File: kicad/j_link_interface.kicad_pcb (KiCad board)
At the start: 4 copper layers, 22.5 x 26.2 mm, 9 parts, among them J1 Conn_01x05_Pin, J2 SSW-110-02-G-D-RA-N, J3 FTSH-107-01-X-DV-K

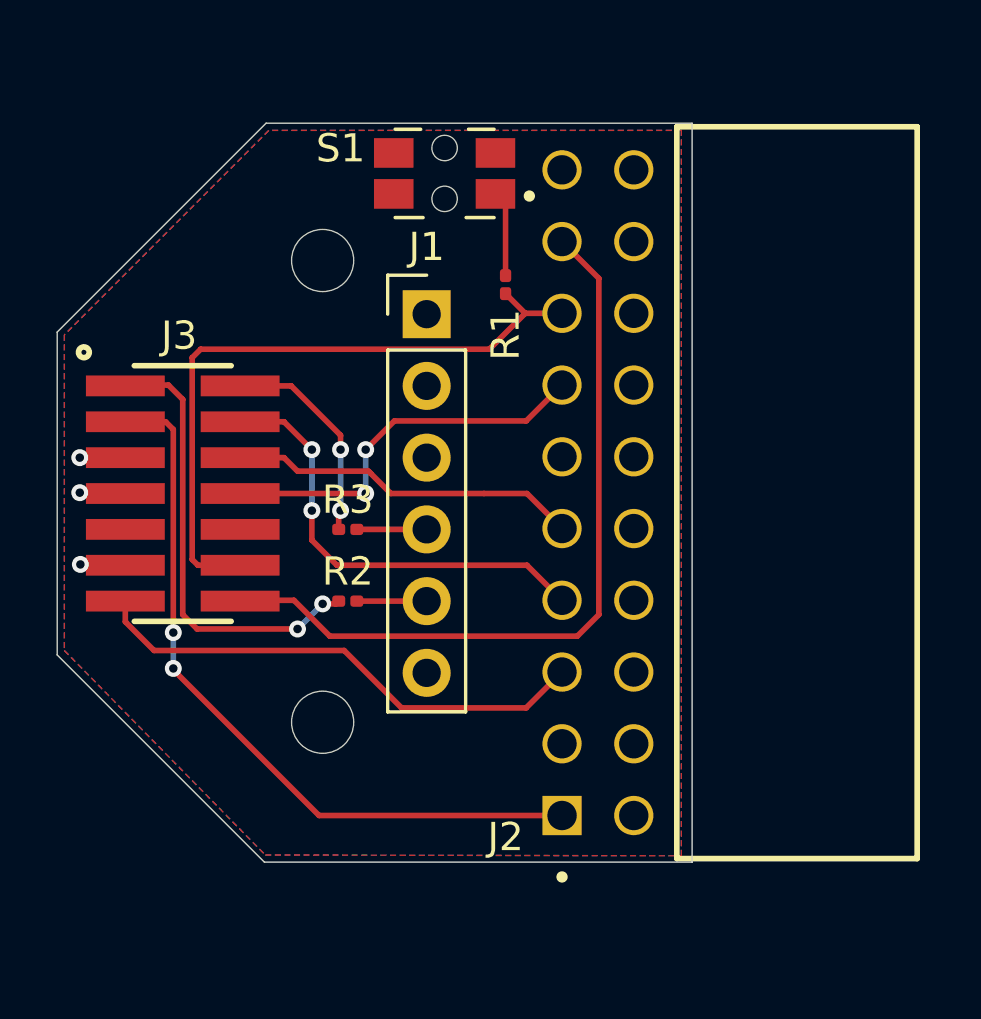
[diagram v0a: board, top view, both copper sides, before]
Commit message: Updated with originally intended 0603 package for resistors. Changed the switch. Changed the IDC connector to a better matching one. Added release workflow.
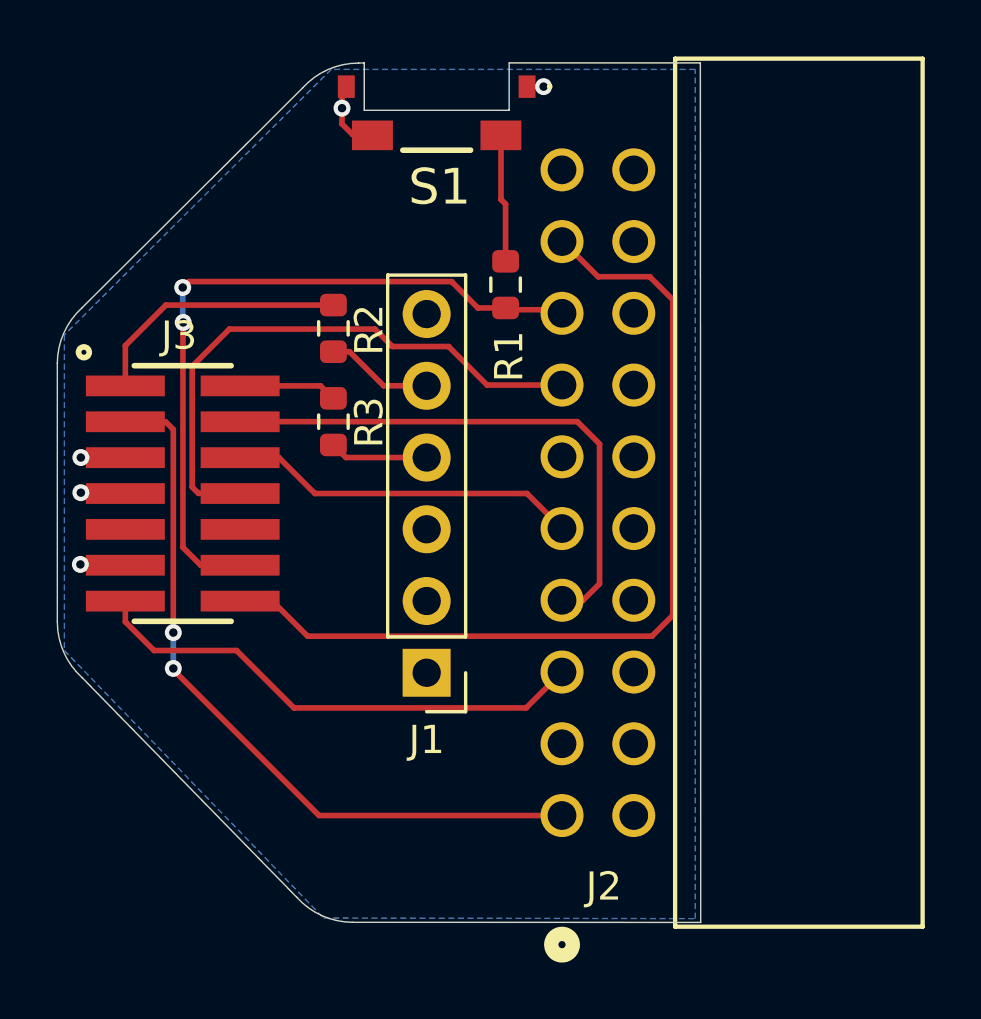
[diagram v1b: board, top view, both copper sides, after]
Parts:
- removed H1, H2: MountingHole, local_library:MountingHole_2.2mm_M2
- J2: value SSW-110-02-G-D-RA-N -> SFH11-PBPC-D10-RA-BK; footprint local_library:SAMTEC_SSW-110-02-G-D-RA-N -> local_library:SFH11-PBPC-D10-RA-BK
- R1, R2, R3: footprint Resistor_SMD:R_0201_0603Metric -> Resistor_SMD:R_0603_1608Metric
- S1: value EVQP7C01P -> ~; footprint local_library:SW_EVQ-P7C01P -> local_library:EVQP4HB3B
- moved J1 12.7 mm to (119.5, 81.9), turned to 180 degrees
- moved R2 9.67 mm to (116.2, 69.7), turned to -90 degrees
- moved S1 3.93 mm to (119.9, 60.3)
- moved R3 3.85 mm to (116.2, 73.1), turned to -90 degrees
- turned J2 to 90 degrees
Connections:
- S1 pad 2: unconnected-(S1-B-Pad2) -> GND
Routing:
- net /SWO: track 13.9 -> 20.5 mm, vias 2 -> 0
- net /FTD_RX: track 16.2 -> 9.61 mm, vias 2 -> 0
- net /VCP_RX: track 27.3 -> 32.1 mm
- net /FTD_TX: track 7.64 -> 3.49 mm, vias 2 -> 0
- net /SWDIO: track 15.9 -> 19.6 mm, vias 2 -> 0
- net GND: track 4.84 -> 8.13 mm, vias 3 -> 5
- net /~{RESET}: track 23.8 -> 25.7 mm, vias 0 -> 2
- net Net-(S1-N.O.): track 3.04 -> 4.55 mm
- net Net-(J1-Pin_5): track 2.47 -> 3.80 mm
- net Net-(J1-Pin_4): track 2.47 -> 3.49 mm
- removed copper zone on F.Cu, net GND
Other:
- board size 22.5 x 26.2 mm -> 22.8 x 30.4 mm
